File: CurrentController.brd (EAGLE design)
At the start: 160 x 100 mm, 137 parts, among them CN1 220uF, CN3 47uF, IC1 LM340S-12, IC2 L7912, IC3 TS514, IC4 MIC5205-5V, IC5 MEGA8-AI, IC6 MIC5205-3V, IC7 PMOS-SOT323, IC8 PMOS-SOT323-SC89, T1 100k, U1 TPS7A470, U2 AD8676, U3 AD8676, U4 NT2006

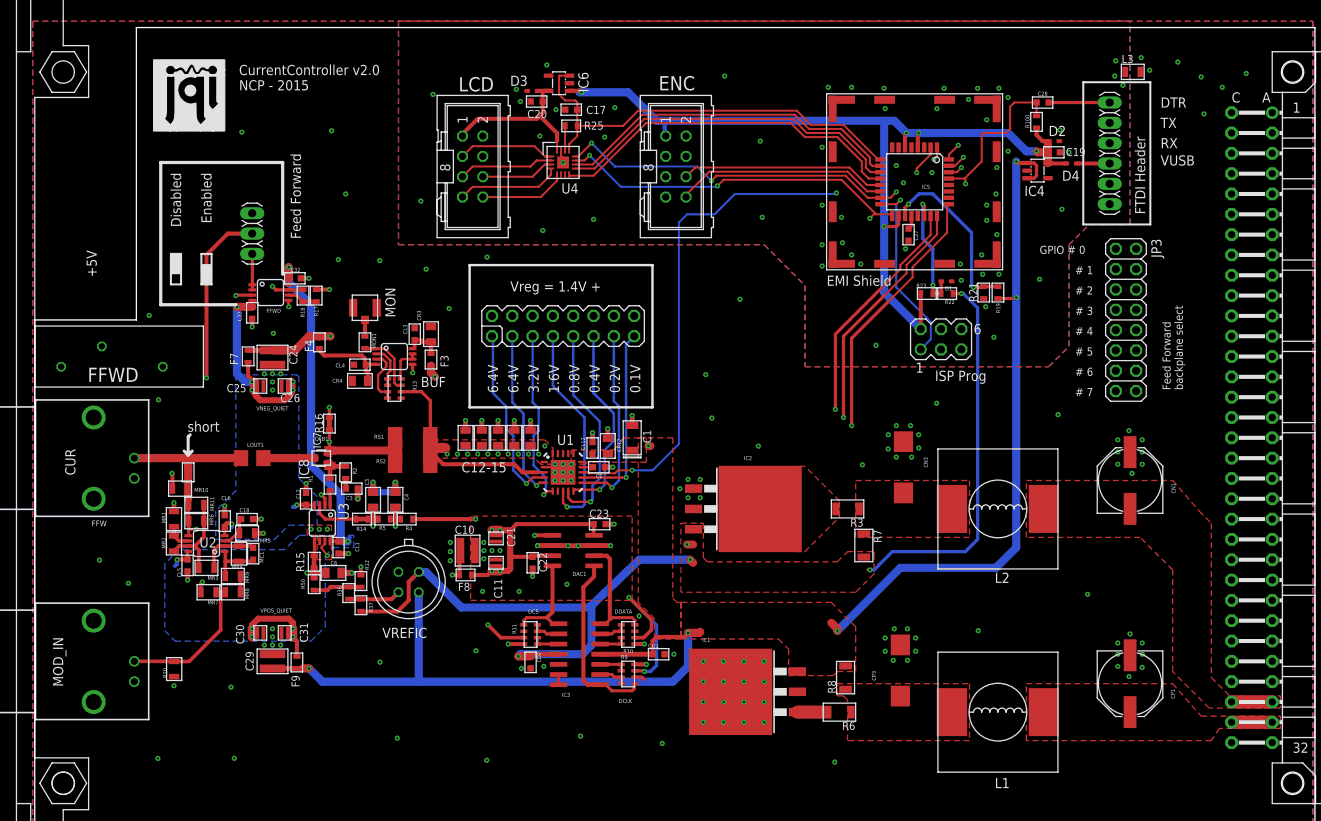
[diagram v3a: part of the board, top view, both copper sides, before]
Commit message: Updated silkscreen; other minor mods
Prepping for fabrication at macrofab.
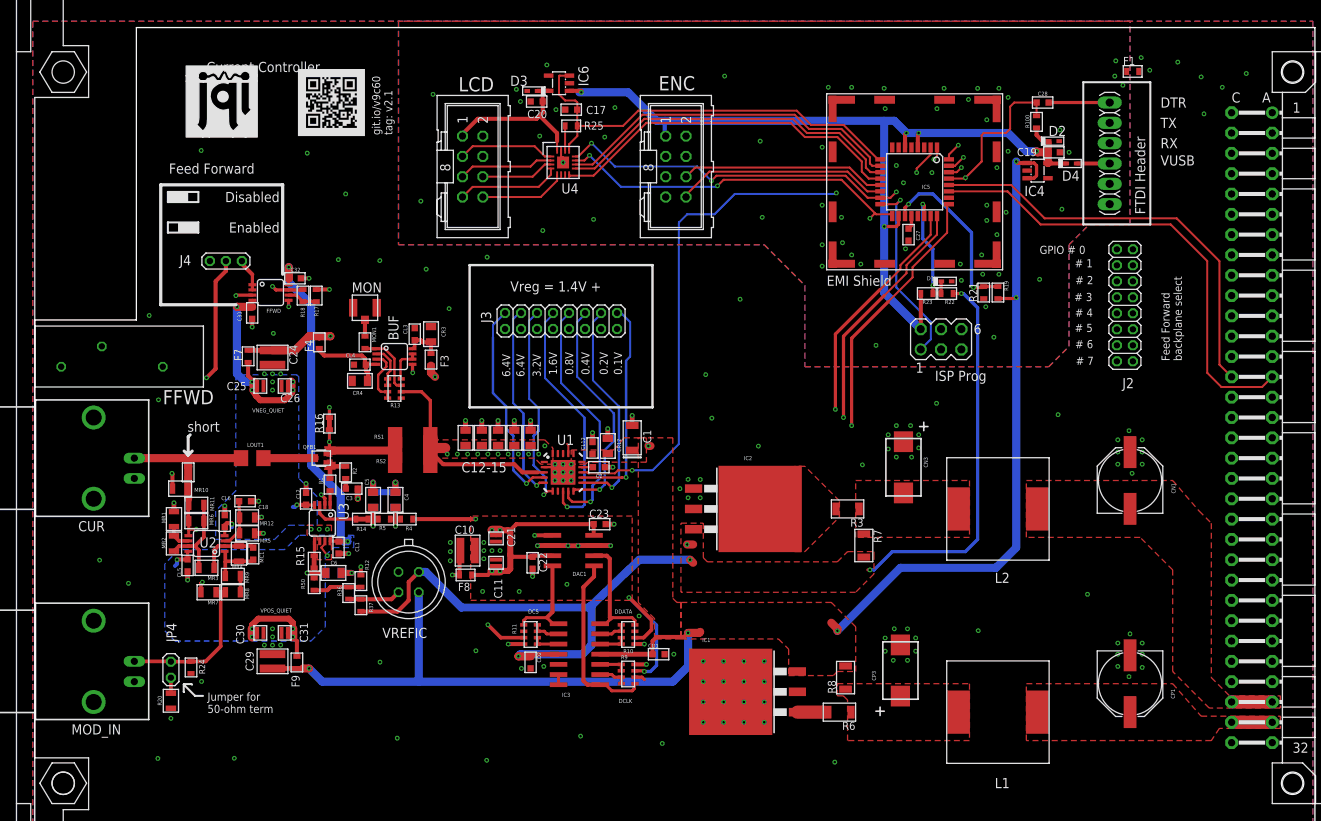
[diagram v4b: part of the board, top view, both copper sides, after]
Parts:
- removed JP2: (no value), pinhead:1X03
- removed JP3: (no value), pinhead:2X08
- removed L3: (no value), jqi_passives:R_0805
- removed SV2: (no value), connector-jqi:MA08-2
- added F1: 1k_ferrite, jqi_passives:L_FERRITE_0603
- added J2, J3: 2X8_LOW_PROFILE_JUMPER, Eurocard-HV-piezo-driver:2X8_LOW_PROFILE_JUMPER_MATRIX
- added J4: 1X3_LOW_PROFILE_JUMPER, pinhead:1X3_LOW_PROFILE
- added JP4: 1X2_LOW_PROFILE_JUMPER, Eurocard-HV-piezo-driver:1X2_LOW_PROFILE
- added MR12: 1k, jqi_passives:R_0805
- added R24: 10k, jqi_passives:R_0603
- added U$6: (no value), QR-git.io-v9c60:QR-HTTPS://GIT.IO/V9C60-LIGHT-SILK
- C18: value (none) -> 1uF
- L1, L2: device jqi_passives:COILCRAFT_MSS1583 -> jqi_passives:WURTH_1280
- moved U$4 4.13 mm to (19.2, 84.6)
- moved R20 3.98 mm to (17.3, 14.1)
- moved C18 2.25 mm to (26.5, 39.1)
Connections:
- new net N$35: JP4.2, R20.P$2
- new net SCL: IC5.28, J1.C14
- new net SDA: IC5.27, J1.A14
- net FEED_FWD: now also J4.P2; no longer JP2.2
- net FFWD: now also J2.P$1, J2.P$11, J2.P$13, J2.P$15, J2.P$3, J2.P$5, J2.P$7, J2.P$9; no longer JP3.1, JP3.11, JP3.13, JP3.15, JP3.3, JP3.5, JP3.7, JP3.9
- net FFWD_POSTGAIN: now also J4.P1; no longer JP2.3
- net GND: now also F1.P$2, J3.P$1, J3.P$11, J3.P$13, J3.P$15, J3.P$3, J3.P$5, J3.P$7, J3.P$9, J4.P3, MR12.P$2, R24.P$1; no longer JP2.1, L3.P$2, SV2.10, SV2.12, SV2.14, SV2.16, SV2.2, SV2.4, SV2.6, SV2.8
- net GPIO0: now also J2.P$2; no longer JP3.2
- net GPIO1: now also J2.P$4; no longer JP3.4
- net GPIO2: now also J2.P$6; no longer JP3.6
- net GPIO3: now also J2.P$8; no longer JP3.8
- net GPIO4: now also J2.P$10; no longer JP3.10
- net GPIO5: now also J2.P$12; no longer JP3.12
- net GPIO6: now also J2.P$14; no longer JP3.14
- net GPIO7: now also J2.P$16; no longer JP3.16
- net MODIN_B: now also JP4.1, R24.P$2; no longer R20.P$2
- net N$19: now also J3.P$2; no longer SV2.1
- net N$21: now also MR12.P$1
- net N$27: now also J3.P$4; no longer SV2.3
- net N$31: now also J3.P$6; no longer SV2.5
- net N$34: now also J3.P$8; no longer SV2.7
- net N$39: now also J3.P$10; no longer SV2.9
- net N$41: now also J3.P$12; no longer SV2.11
- net N$43: now also J3.P$14; no longer SV2.13
- net N$44: now also J3.P$16; no longer SV2.15
- net VSS: now also F1.P$1; no longer L3.P$1
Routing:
- net SDA: track 0.00 -> 59.3 mm
- net SCL: track 0.00 -> 52.9 mm
- net FEED_FWD: track 37.8 -> 31.3 mm
- net N$43: track 23.6 -> 28.0 mm
- net N$41: track 24.3 -> 28.5 mm
- net N$39: track 26.4 -> 30.3 mm
- net N$34: track 27.2 -> 30.9 mm
- net N$44: track 23.6 -> 27.3 mm
- net N$31: track 22.4 -> 25.9 mm
- net N$19: track 22.7 -> 26.2 mm
- net N$27: track 21.0 -> 24.4 mm
- net N$21: track 4.12 -> 6.35 mm
- net GND: track 24.2 -> 26.4 mm, vias 135 -> 136
- net N$35: track 0.00 -> 1.94 mm
- net FFWD: track 147.8 -> 145.9 mm
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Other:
- board text added: "Current Controller"
- board text added: "Jumper for 50-ohm term"
- board text added: "git.io/v9c60 tag: v2.1"
- board text removed: "+5V"
- board text removed: "CurrentController v2.0 NCP - 2015"
- board text removed: "FFW"
